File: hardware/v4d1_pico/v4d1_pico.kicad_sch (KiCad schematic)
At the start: 107 parts, among them J1 joystick, J10 ON/OFF, J11 MIDI IN bk: 5 R: 4, J2 LED strip, J3 SSD1306 SPI, J4 MIDI OUT Y:M5 - R:M4, J5 Batt, J6 Neck - Y:O BK:B R:3.3, J7 01x03, J8 MXP5010, J9 Thumb, Q1 2N7000, SW1 SW_DIP_x01, U1 74HC165, U2 74HC165, U3 74HC165, U4 Pico, U5 FJ08K, U6 6N138, U7 MCP3002

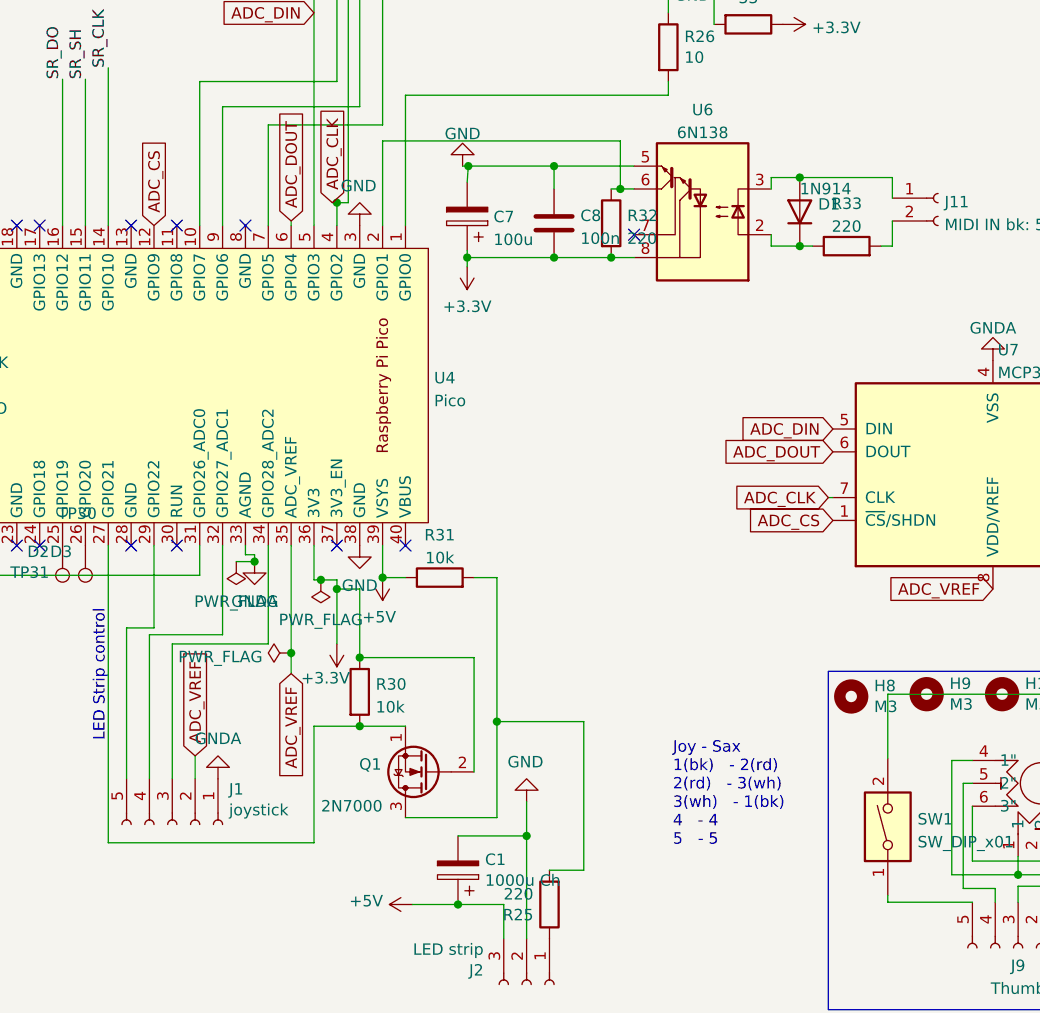
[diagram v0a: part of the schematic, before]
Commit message: Updated PCB with bite sensor
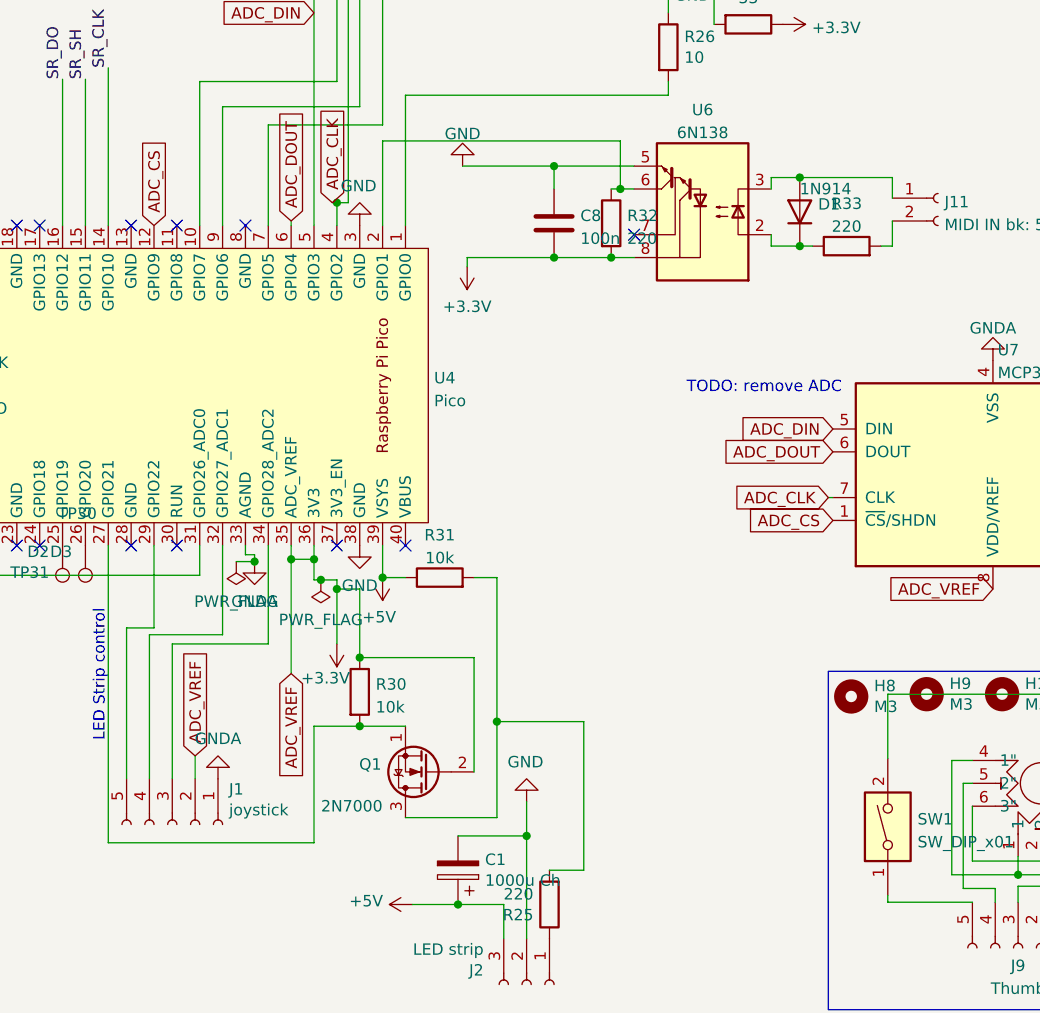
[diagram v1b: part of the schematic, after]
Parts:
- removed C7: 100u, Capacitor_THT:CP_Radial_D6.3mm_P2.50mm, symbol Device:C_Polarized
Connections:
- net ADC_VREF is gone; now on net +3.3V: C5.1, J1.2 (Pin_2), J6.3 (Pin_3), U4.35 (ADC_VREF), U7.8 (VDD/VREF)
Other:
- note added: "TODO: remove ADC"
- note removed: "Joy - Sax 1(bk) - 2(rd) 2(rd) - 3(wh) 3(wh) - 1(bk) 4 - 4 5 - 5"
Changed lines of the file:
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@@
   (junction (at 48.26 106.68) (diameter 0) (color 0 0 0 0)
   )
-  (junction (at 174.498 76.708) (diameter 0) (color 0 0 0 0)
+  (junction (at 154.94 110.236) (diameter 0) (color 0 0 0 0)
   )
   (junction (at 158.242 112.522) (diameter 0) (color 0 0 0 0)
@@
   (junction (at 58.42 167.64) (diameter 0) (color 0 0 0 0)
   )
+  (junction (at 157.48 110.236) (diameter 0) (color 0 0 0 0)
+  )
   (junction (at 19.05 121.92) (diameter 0) (color 0 0 0 0)
   )
   (junction (at 271.526 28.956) (diameter 0) (color 0 0 0 0)
   )
-  (junction (at 174.625 66.548) (diameter 0) (color 0 0 0 0)
-  )
   (junction (at 240.792 145.288) (diameter 0) (color 0 0 0 0)
   )
@@
   (junction (at 36.83 43.18) (diameter 0) (color 0 0 0 0)
   )
-  (junction (at 154.94 120.65) (diameter 0) (color 0 0 0 0)
-  )
   (junction (at 270.256 138.938) (diameter 0) (color 0 0 0 0)
   )
@@
     (stroke (width 0) (type default) (color 0 0 0 0))
   )
-  (wire (pts (xy 154.94 122.936) (xy 154.94 120.65))
-    (stroke (width 0) (type default) (color 0 0 0 0))
-  )
   (wire (pts (xy 66.04 162.56) (xy 68.58 162.56))
     (stroke (width 0) (type default) (color 0 0 0 0))
@@
     (stroke (width 0) (type default) (color 0 0 0 0))
   )
+  (wire (pts (xy 154.94 110.236) (xy 157.48 110.236))
+    (stroke (width 0) (type default) (color 0 0 0 0))
+  )
   (polyline (pts (xy 214.63 122.682) (xy 249.936 122.682))
     (stroke (width 0) (type default) (color 0 0 0 0))
@@
     (stroke (width 0) (type default) (color 0 0 0 0))
   )
-  (wire (pts (xy 174.625 66.548) (xy 184.15 66.548))
+  (wire (pts (xy 173.99 66.548) (xy 184.15 66.548))
     (stroke (width 0) (type default) (color 0 0 0 0))
   )
@@
     (stroke (width 0) (type default) (color 0 0 0 0))
   )
+  (wire (pts (xy 154.94 110.236) (xy 154.94 108.712))
+    (stroke (width 0) (type default) (color 0 0 0 0))
+  )
   (wire (pts (xy 132.08 56.896) (xy 132.08 73.152))
     (stroke (width 0) (type default) (color 0 0 0 0))
@@
     (stroke (width 0) (type default) (color 0 0 0 0))
   )
-  (wire (pts (xy 157.48 108.712) (xy 157.48 112.522))
+  (wire (pts (xy 157.48 108.712) (xy 157.48 110.236))
     (stroke (width 0) (type default) (color 0 0 0 0))
   )
@@
     (stroke (width 0) (type default) (color 0 0 0 0))
   )
-  (wire (pts (xy 174.625 66.548) (xy 174.498 68.326))
-    (stroke (width 0) (type default) (color 0 0 0 0))
-  )
   (wire (pts (xy 265.176 126.238) (xy 265.176 131.318))
     (stroke (width 0) (type default) (color 0 0 0 0))
@@
     (stroke (width 0) (type default) (color 0 0 0 0))
   )
+  (wire (pts (xy 157.48 110.236) (xy 157.48 112.522))
+    (stroke (width 0) (type default) (color 0 0 0 0))
+  )
   (wire (pts (xy 167.64 58.674) (xy 196.85 58.674))
     (stroke (width 0) (type default) (color 0 0 0 0))
@@
     (stroke (width 0) (type default) (color 0 0 0 0))
   )
-  (wire (pts (xy 173.99 66.548) (xy 174.625 66.548))
-    (stroke (width 0) (type default) (color 0 0 0 0))
-  )
   (wire (pts (xy 177.8 112.268) (xy 177.8 128.27))
     (stroke (width 0) (type default) (color 0 0 0 0))
@@
     (stroke (width 0) (type default) (color 0 0 0 0))
   )
-  (wire (pts (xy 154.94 120.65) (xy 154.94 108.712))
+  (wire (pts (xy 154.94 110.236) (xy 154.94 122.936))
     (stroke (width 0) (type default) (color 0 0 0 0))
   )
@@
     (stroke (width 0) (type default) (color 0 0 0 0))
   )
-  (wire (pts (xy 174.498 75.946) (xy 174.498 76.708))
-    (stroke (width 0) (type default) (color 0 0 0 0))
-  )
   (wire (pts (xy 49.53 101.6) (xy 44.45 101.6))
     (stroke (width 0) (type default) (color 0 0 0 0))
@@
     (effects (font (size 1.27 1.27)) (justify left bottom))
   )
-  (text "Beak PCB\n" (at 273.558 120.396 0)
+  (text "TODO: remove ADC" (at 198.882 91.948 0)
     (effects (font (size 1.27 1.27)) (justify left bottom))
   )
-  (text "LED Strip control" (at 134.366 130.556 90)
+  (text "Beak PCB\n" (at 273.558 120.396 0)
     (effects (font (size 1.27 1.27)) (justify left bottom))
   )
-  (text "Joy - Sax\n1(bk)   - 2(rd)\n2(rd)   - 3(wh)\n3(wh)   - 1(bk)\n4   - 4\n5   - 5\n"
-    (at 197.358 142.24 0)
+  (text "LED Strip control" (at 134.366 130.556 90)
     (effects (font (size 1.27 1.27)) (justify left bottom))
   )
@@
     (pin "2")
   )
-  (symbol (lib_id "power:PWR_FLAG") (at 154.94 120.65 90) (unit 1)
-    (in_bom yes) (on_board yes) (fields_autoplaced)
-    (property "Reference" "#FLG0105" (id 0) (at 153.035 120.65 0)
-      (effects (font (size 1.27 1.27)) hide)
-    )
-    (property "Value" "PWR_FLAG" (id 1) (at 151.7651 121.0838 90)
-      (effects (font (size 1.27 1.27)) (justify left))
-    )
-    (property "Footprint" "" (id 2) (at 154.94 120.65 0)
-      (effects (font (size 1.27 1.27)) hide)
-    )
-    (property "Datasheet" "~" (id 3) (at 154.94 120.65 0)
-      (effects (font (size 1.27 1.27)) hide)
-    )
-    (pin "1")
-  )
   (symbol (lib_id "Mechanical:MountingHole") (at 163.068 187.198 0) (unit 1)
     (in_bom yes) (on_board yes)
@@
     (pin "1")
   )
-  (symbol (lib_id "Device:C_Polarized") (at 174.498 72.136 180) (unit 1)
-    (in_bom yes) (on_board yes) (fields_autoplaced)
-    (property "Reference" "C7" (id 0) (at 177.419 72.1903 0)
-      (effects (font (size 1.27 1.27)) (justify right))
-    )
-    (property "Value" "100u" (id 1) (at 177.419 74.7272 0)
-      (effects (font (size 1.27 1.27)) (justify right))
-    )
-    (property "Footprint" "Capacitor_THT:CP_Radial_D6.3mm_P2.50mm" (id 2) (at 173.5328 68.326 0)
-      (effects (font (size 1.27 1.27)) hide)
-    )
-    (property "Datasheet" "~" (id 3) (at 174.498 72.136 0)
-      (effects (font (size 1.27 1.27)) hide)
-    )
-    (pin "1")
-    (pin "2")
-  )
   (symbol (lib_id "Device:C") (at 260.096 140.208 0) (unit 1)
     (in_bom yes) (on_board yes) (fields_autoplaced)
@@
       (reference "#FLG0104") (unit 1) (value "PWR_FLAG") (footprint "")
     )
-    (path "/2b6fe08e-215a-48de-befd-492d522b663d"
-      (reference "#FLG0105") (unit 1) (value "PWR_FLAG") (footprint "")
-    )
     (path "/bdc071c1-ead1-4ebf-a5f2-186ad8777b92"
       (reference "#PWR01") (unit 1) (value "GNDA") (footprint "")
@@
       (reference "C6") (unit 1) (value "470p") (footprint "Capacitor_THT:C_Disc_D3.4mm_W2.1mm_P2.50mm")
     )
-    (path "/7645b832-44a0-4178-932a-e01c230c6392"
-      (reference "C7") (unit 1) (value "100u") (footprint "Capacitor_THT:CP_Radial_D6.3mm_P2.50mm")
-    )
     (path "/6ea2bc83-6e60-44b0-9fd6-b93a1503a50c"
